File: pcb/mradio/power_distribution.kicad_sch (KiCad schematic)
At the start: 52 parts, among them U201 TXB0108PW, U202 TPS7A8500ARGRR, U203 TPS54560BDDA, U204 TPS54560BDDA

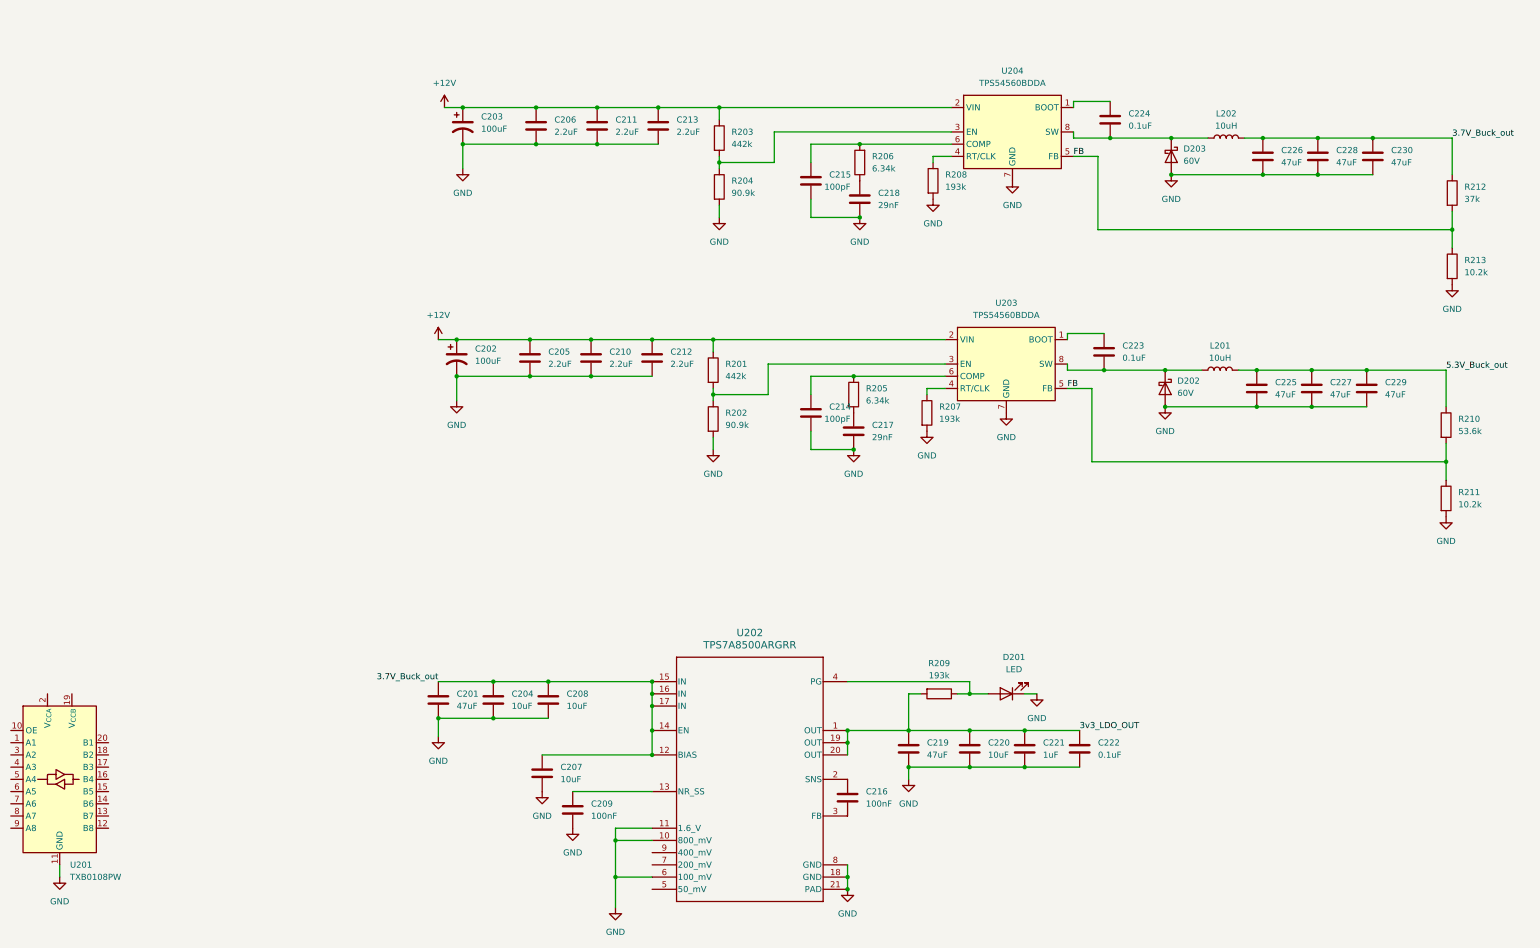
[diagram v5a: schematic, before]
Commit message: Separated converters, 5V and 3v3 lines done
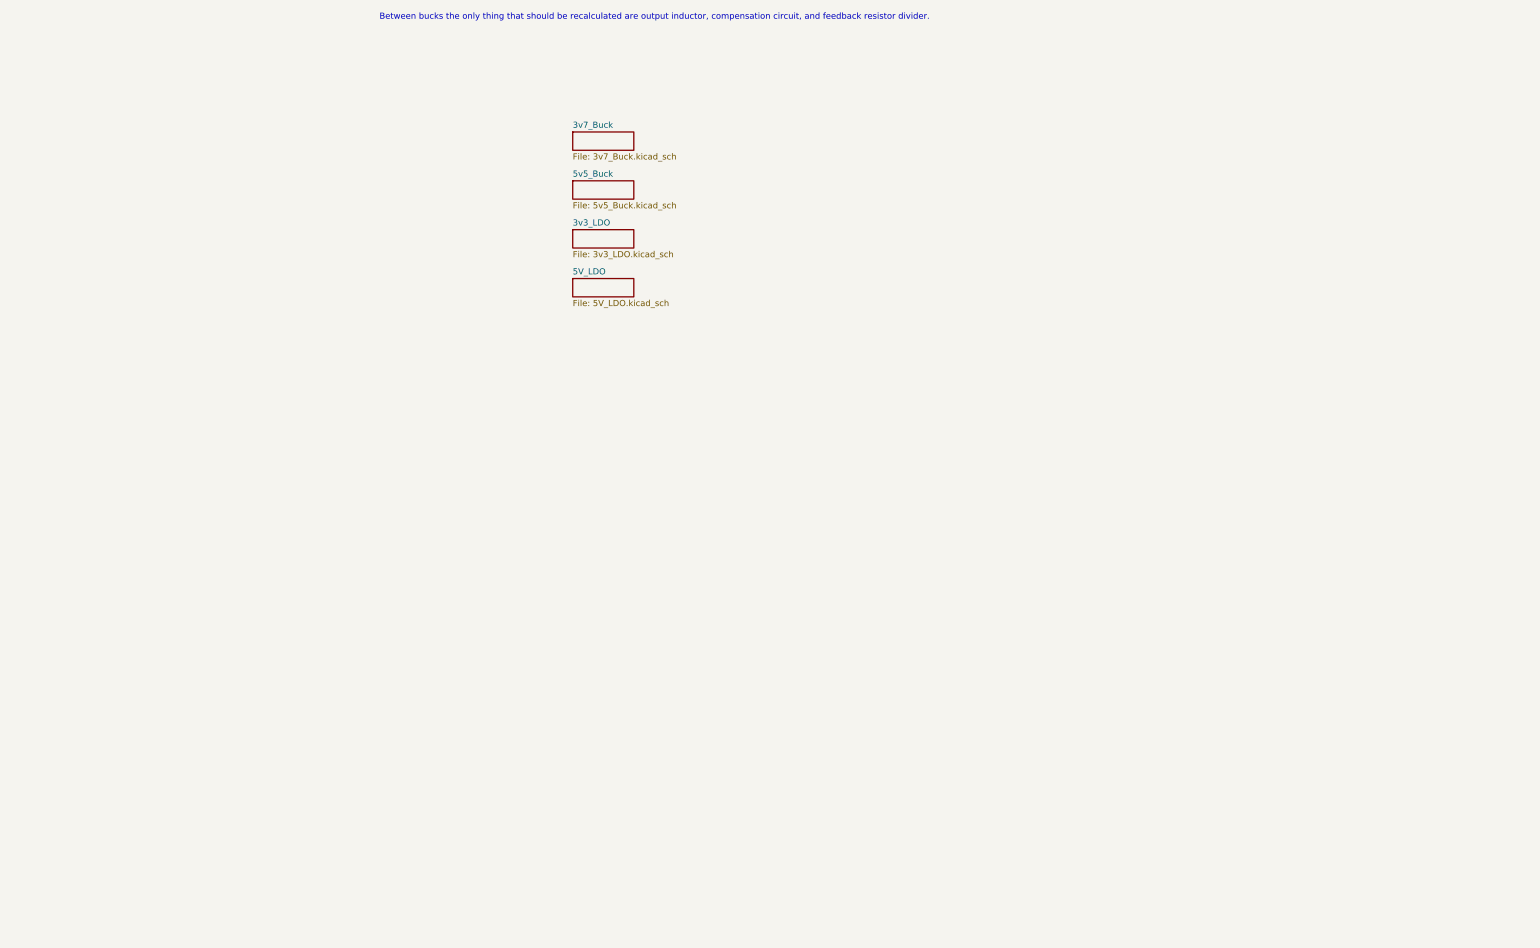
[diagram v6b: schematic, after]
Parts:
- removed C201: 47uF, RGR0020A, symbol Device:C
- removed C202, C203: 100uF, symbol Device:C_Polarized_US
- removed C204, C207, C208: 10uF, RGR0020A, symbol Device:C
- removed C205, C206, C210, C211, C212, C213: 2.2uF, symbol Device:C
- removed C209, C216: 100nF, symbol Device:C
- removed C214, C215: 100pF, symbol Device:C
- removed C217, C218: 29nF, symbol Device:C
- removed C219, C225, C226, C227, C228, C229, C230: 47uF, symbol Device:C
- removed C220: 10uF, symbol Device:C
- removed C221: 1uF, symbol Device:C
- removed C222, C223, C224: 0.1uF, symbol Device:C
- removed D201: LED, symbol Device:LED
- removed D202, D203: 60V, symbol Device:D_Schottky
- removed L201, L202: 10uH, symbol Device:L
- removed R201, R203: 442k, symbol Device:R
- removed R202, R204: 90.9k, symbol Device:R
- removed R205, R206: 6.34k, symbol Device:R
- removed R207, R208, R209: 193k, symbol Device:R
- removed R210: 53.6k, symbol Device:R
- removed R211, R213: 10.2k, symbol Device:R
- removed R212: 37k, symbol Device:R
- removed U201: TXB0108PW, Package_SO:TSSOP-20_4.4x6.5mm_P0.65mm, symbol Logic_LevelTranslator:TXB0108PW
- removed U202: TPS7A8500ARGRR, RGR0020A, symbol symbols:TPS7A8500ARGRR
- removed U203, U204: TPS54560BDDA, Package_SO:Texas_R-PDSO-G8_EP2.95x4.9mm_Mask2.4x3.1mm_ThermalVias, symbol Regulator_Switching:TPS54560BDDA
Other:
- added sheet 3v3_LDO (3v3_LDO.kicad_sch)
- added sheet 3v7_Buck (3v7_Buck.kicad_sch)
- added sheet 5V_LDO (5V_LDO.kicad_sch)
- added sheet 5v5_Buck (5v5_Buck.kicad_sch)
- note added: "Between bucks the only thing that should be recalculated are output inductor, compensation circuit, and feedback resistor divider."

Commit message: Voltage conversion
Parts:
- added J1: 2125280201, CONN_2125280000_02_MOL, symbol symbols:2125280201
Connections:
- new net +12V: J1.1
- new net GND: J1.2
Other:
- sheet 5v5_Buck renamed 2v2_Buck
- added sheet 1v8_LDO (1v8_LDO.kicad_sch)
